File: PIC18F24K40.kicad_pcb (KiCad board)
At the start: 2 copper layers, 22 x 34.5 mm, 15 parts, among them J1 Conn_01x13, J2 Conn_01x13, J3 ICSP, J4 USB_B_Micro, U1 FT231XQ, U2 PIC18F24K40-I_ML

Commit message: Logo added; fab outputs generated
I've added a test logo to the back silkscreen to see how the
manufacturer does.
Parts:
- added G***: LOGO, _PIC18F24K40:test, B.Cu at (115.6, 91.2)
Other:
- rule pad_to_mask_clearance: 0.051 -> 0
- rule solder_mask_min_width: 0.25 -> 0.2

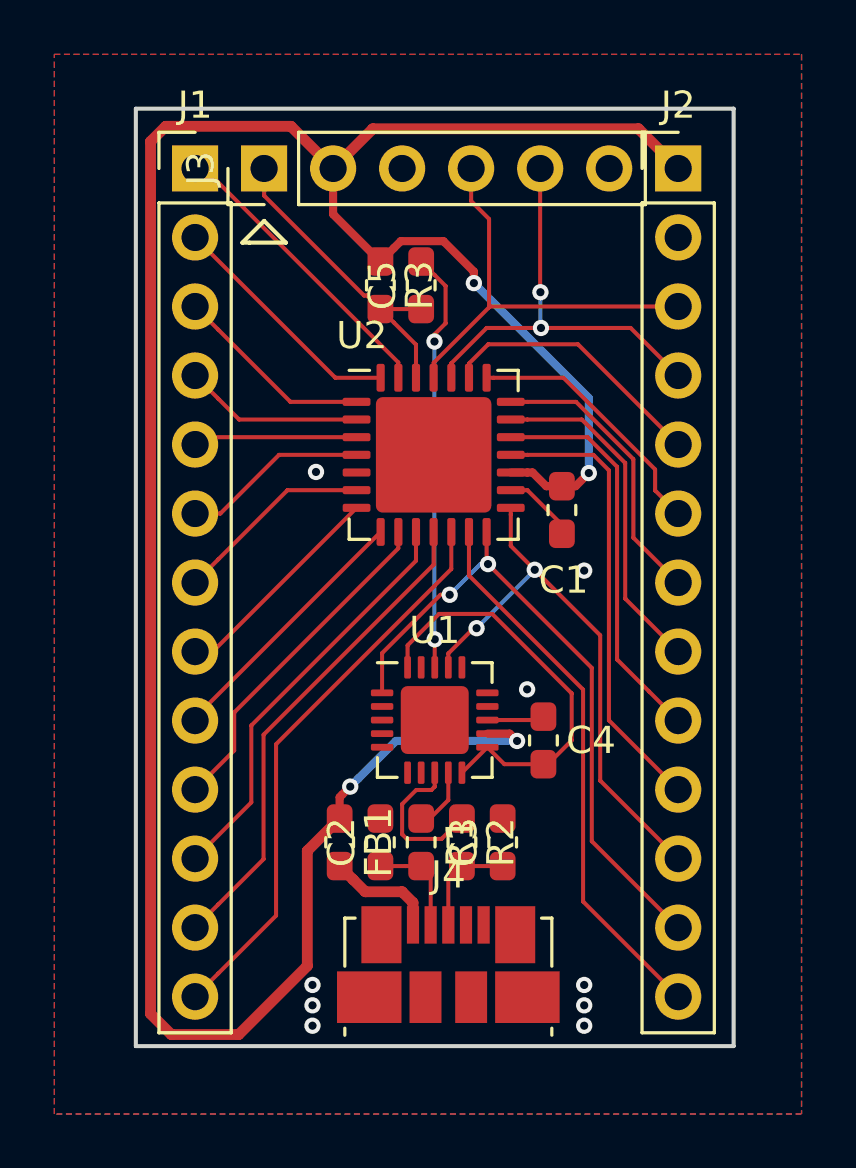
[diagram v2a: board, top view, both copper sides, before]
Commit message: Reset button added Designators hidden
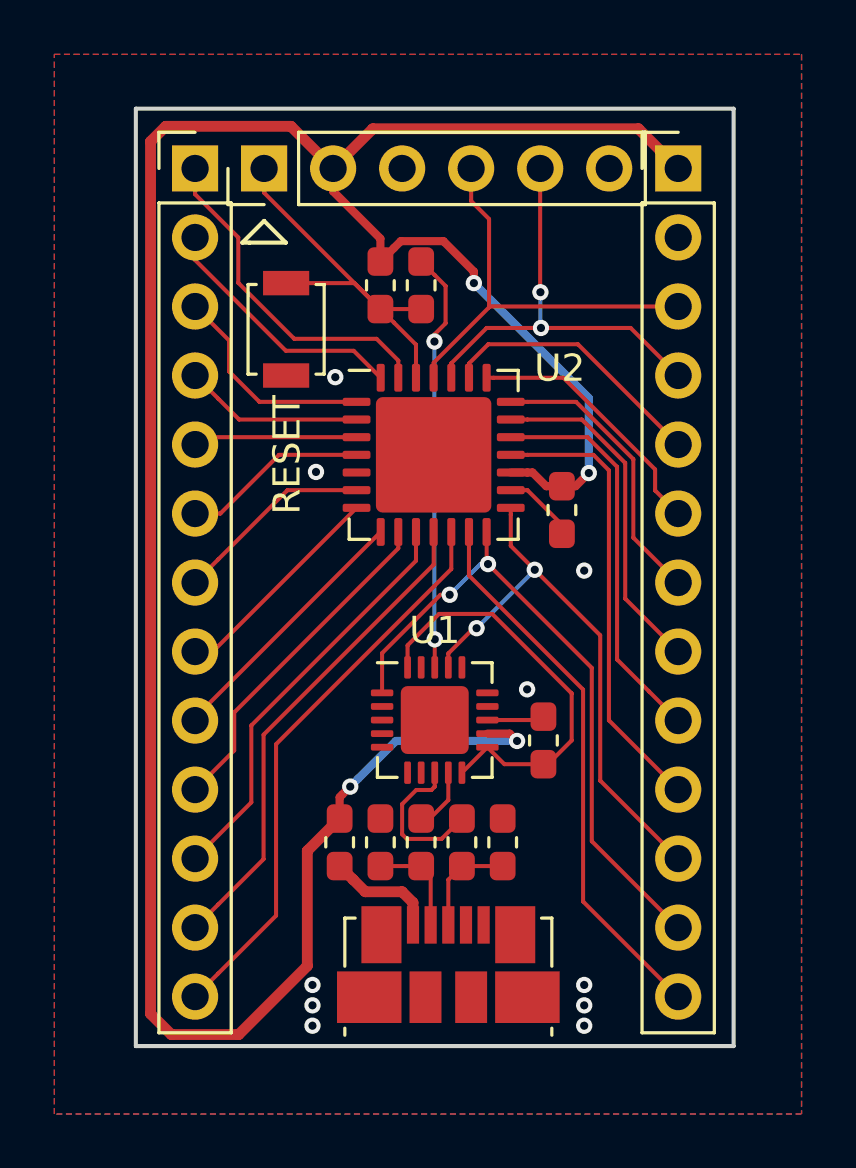
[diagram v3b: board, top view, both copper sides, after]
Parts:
- removed G***: LOGO, _PIC18F24K40:test
- added SW1: SW_SPST, _PIC18F24K40:SW_SPST_B3U-1000P, F.Cu at (110.0, 82.1)
- FB1: value TBD -> 330 Ohms @ 100MHz
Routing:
- net /RE3: track 11.6 -> 15.4 mm
- net /RA0: track 11.0 -> 12.6 mm
- net /RA2: track 7.40 -> 8.06 mm
- net GND: vias 9 -> 10
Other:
- board text added: "RESET"
